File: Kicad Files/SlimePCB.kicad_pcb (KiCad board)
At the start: 2 copper layers, 60 x 50 mm, 9 parts, among them J1 JST 5Pin XH 2.54mm, SW1 SS12D10, U1 WeMos_D1_mini

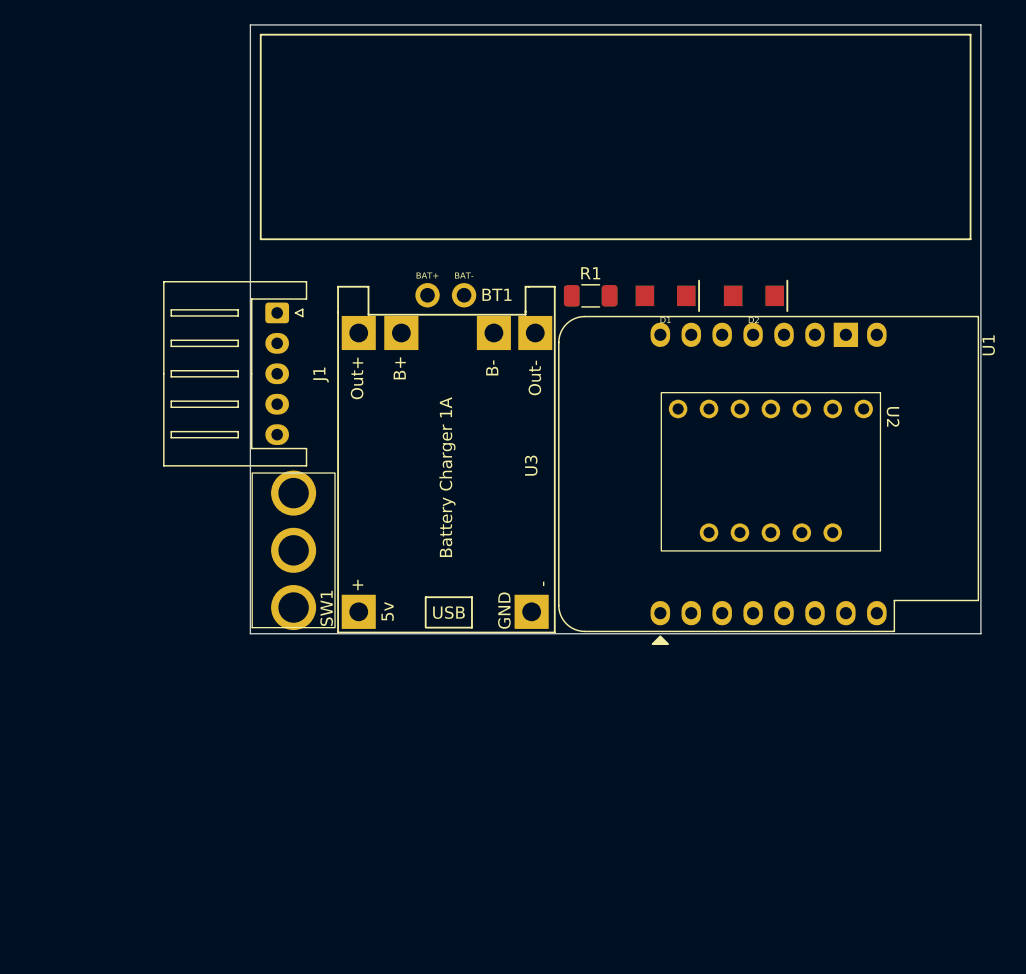
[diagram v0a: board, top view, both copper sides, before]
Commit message: Changed layout
Things to do
Learn how to add ground pours, signal return paths, stitching vias, ground vias
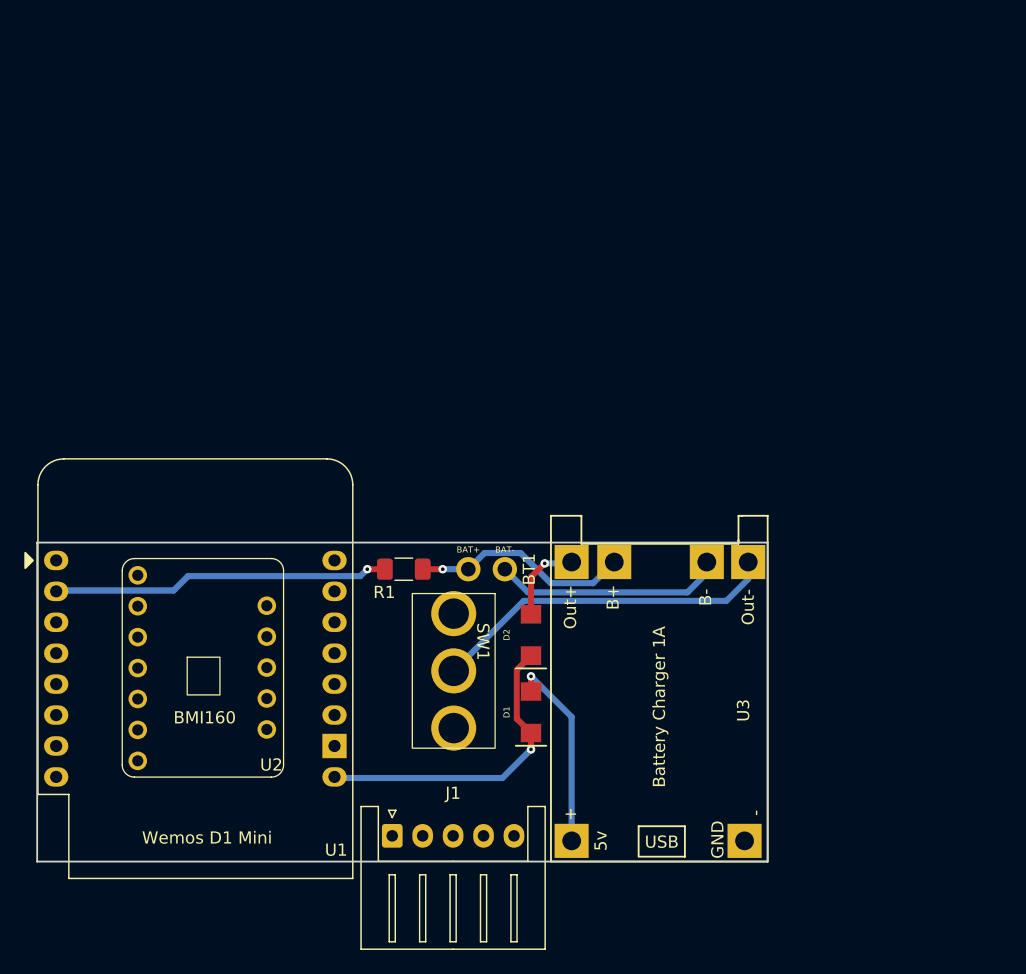
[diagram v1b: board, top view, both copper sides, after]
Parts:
- moved U2 53.7 mm to (130.0, 122.1), turned to 0 degrees
- moved U1 49.8 mm to (124.5, 122.2), turned to 0 degrees
- moved J1 44.0 mm to (152.2, 144.8), turned to 0 degrees
- moved D1 35.9 mm to (163.6, 134.7), turned to 90 degrees
- moved D2 33.3 mm to (163.6, 128.3), turned to 90 degrees
- moved R1 27.2 mm to (153.1, 123.0), turned to 180 degrees
- moved U3 25.7 mm to (165.2, 147.0)
- moved BT1 22.7 mm to (159.9, 123.0)
- moved SW1 16.2 mm to (157.1, 131.2), turned to -90 degrees
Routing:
- net Net-(SW1-B): track 0.00 -> 28.7 mm
- net Net-(U1-A0): track 0.00 -> 27.9 mm, vias 0 -> 1
- net Net-(D1-K): track 0.00 -> 25.8 mm, vias 0 -> 1
- net Net-(BT1-Bat-): track 0.00 -> 18.9 mm
- net Net-(BT1-Bat+): track 0.00 -> 18.1 mm, vias 0 -> 1
- net Net-(U3-RB+): track 0.00 -> 16.4 mm, vias 0 -> 1
- net Net-(U3-Out+): track 0.00 -> 6.90 mm, vias 0 -> 1
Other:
- board size 60 x 50 mm -> 60 x 26.2 mm
